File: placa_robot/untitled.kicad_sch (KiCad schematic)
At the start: 9 parts, among them U1 LMV324, U2 LMV324

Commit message: test_point
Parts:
- added TP3, TP4, TP5, TP6, TP7, TP8, TP9: TestPoint, symbol Connector:TestPoint
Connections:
- net VCC is gone; now on net +3.3V: S1.13 (3'), S1.3
- net +3.3V: now also TP3.1, TP6.1, TP7.1
- net Joystick_D: now also TP8.1
- net Joystick_Down: now also TP5.1
- net Joystick_Left: now also TP9.1
- net Joystick_Up: now also TP4.1

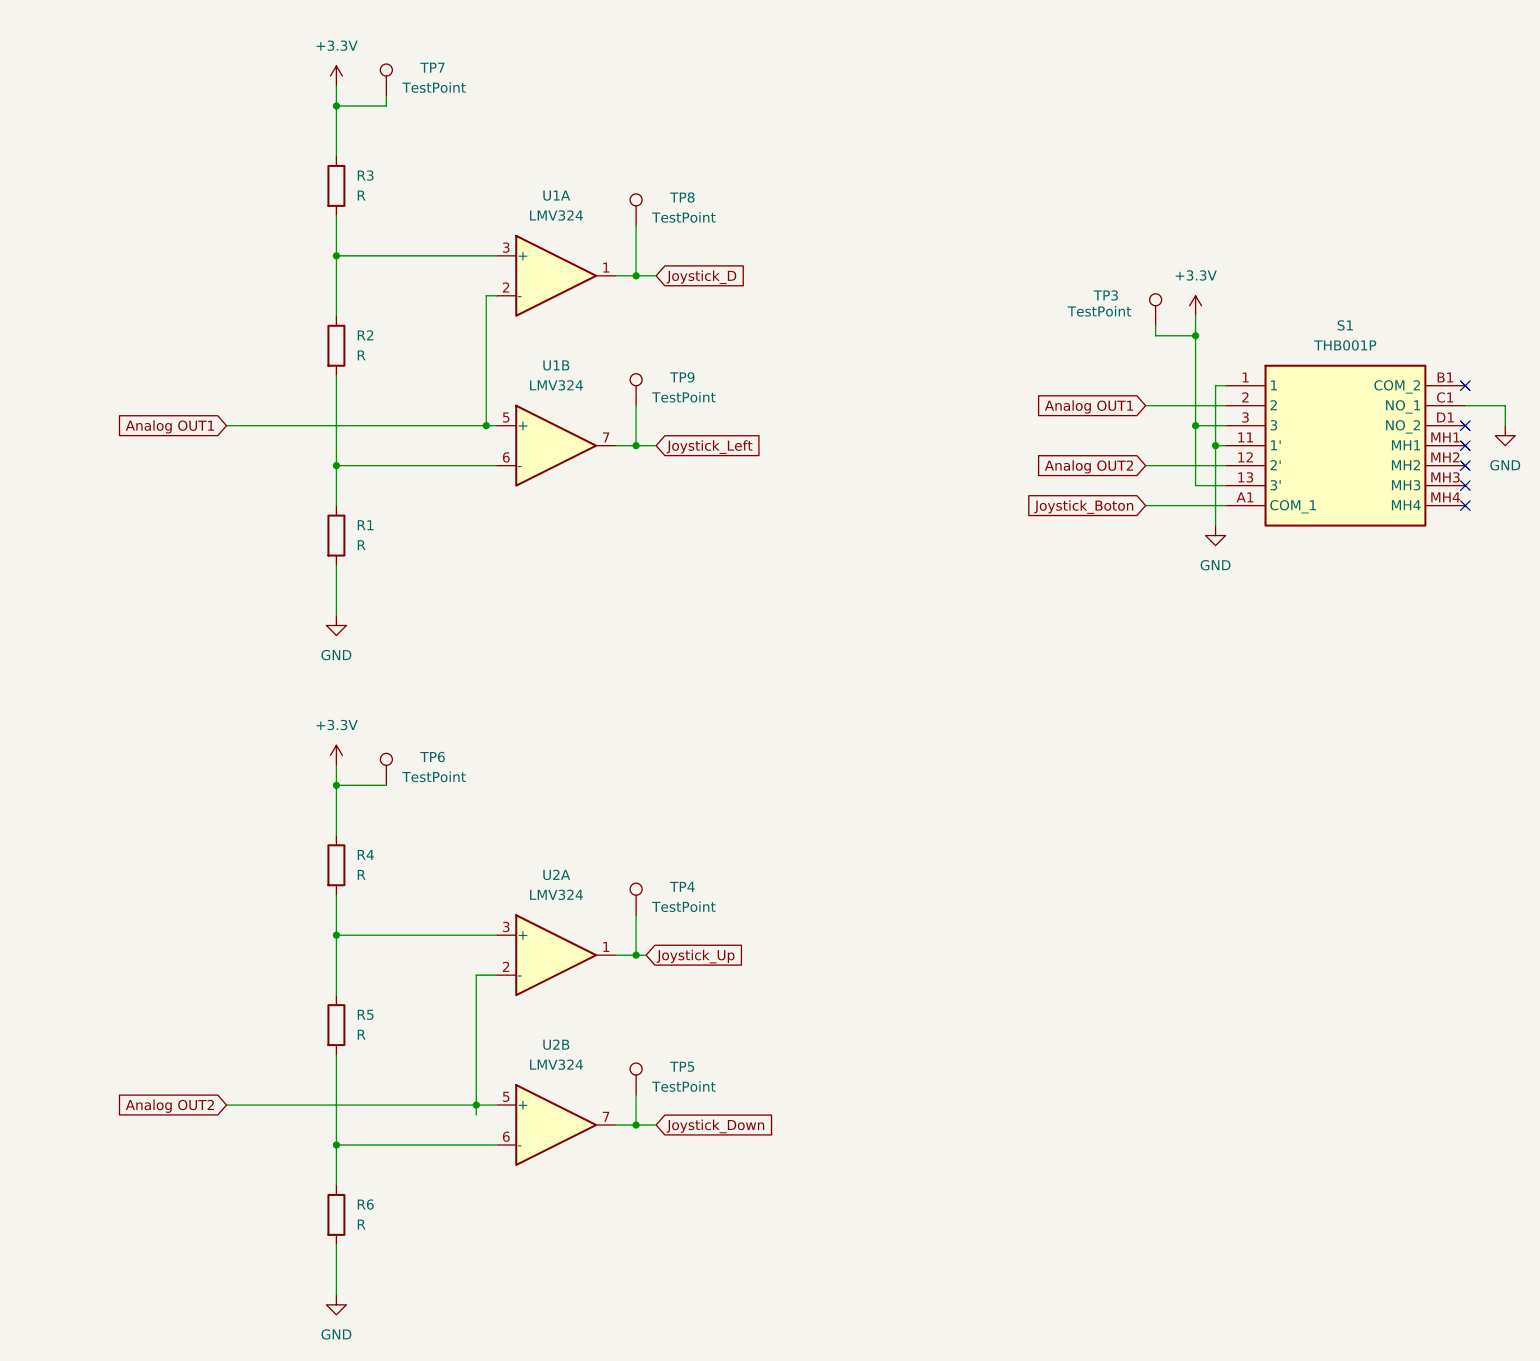
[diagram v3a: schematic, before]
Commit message: Cambio joystick
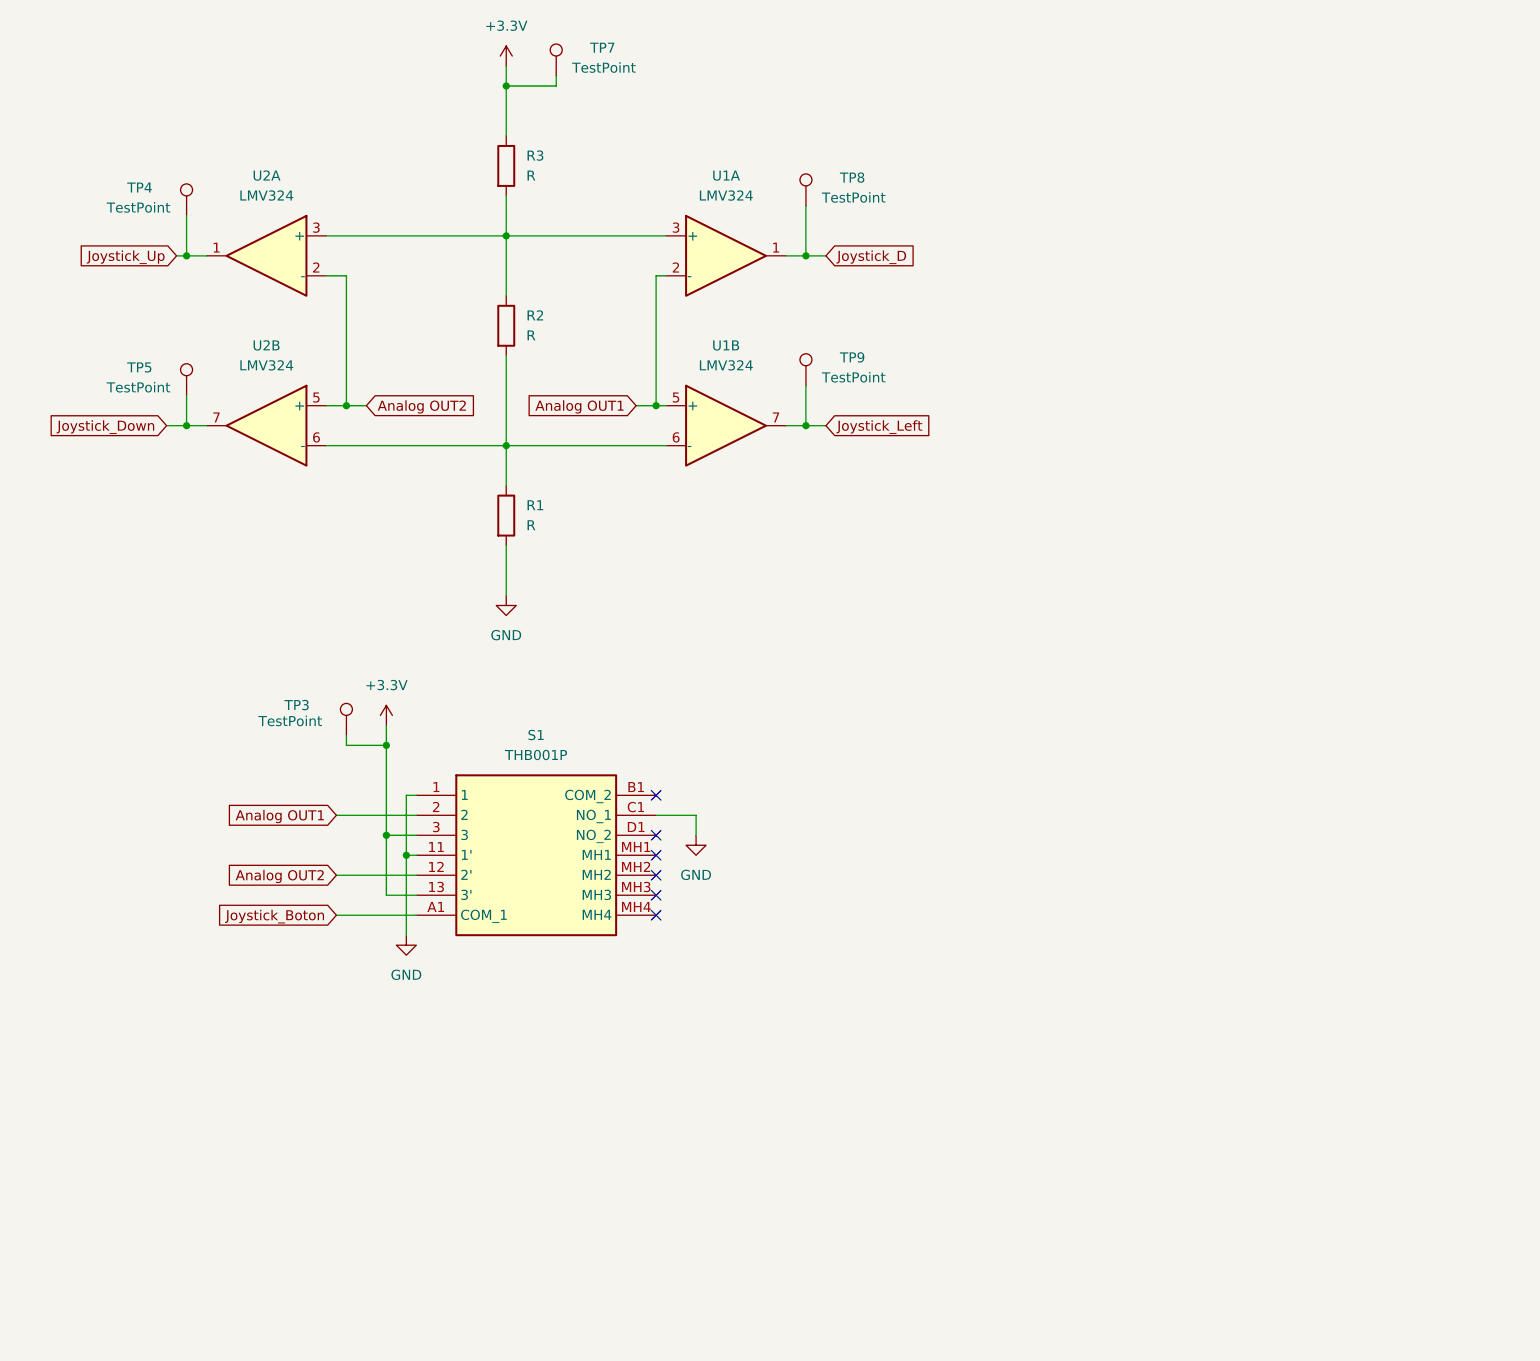
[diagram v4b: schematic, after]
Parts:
- removed R4, R5, R6: R, symbol Device:R
- removed TP6: TestPoint, symbol Connector:TestPoint
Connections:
- net at R2.1, R3.2, U1.3 (+): now also U2.3 (+)
- net at U2.6 (-): now also R1.1, R2.2, U1.6 (-)
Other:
- moved on the sheet: R1, R2, R3, S1, TP3, TP4, TP5, TP7, TP8, TP9, U1A, U1B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
